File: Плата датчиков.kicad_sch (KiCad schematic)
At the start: 0 parts

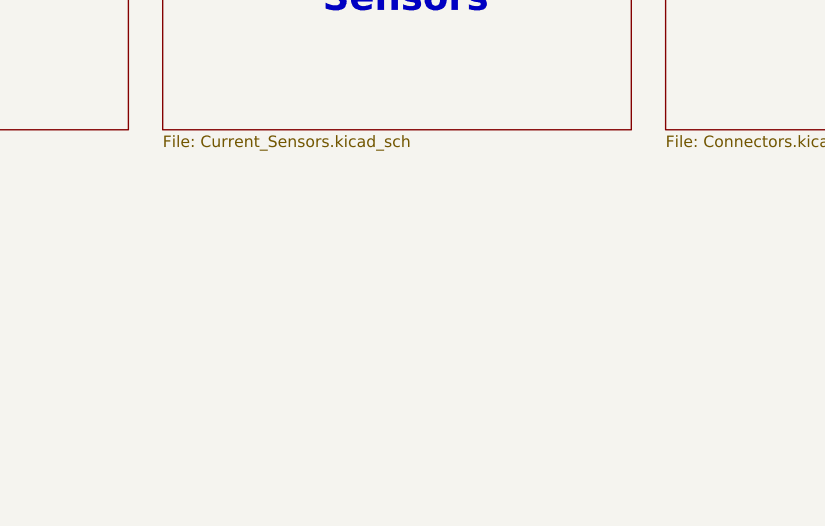
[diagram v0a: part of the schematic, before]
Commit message: Переместил силовые разъёмы
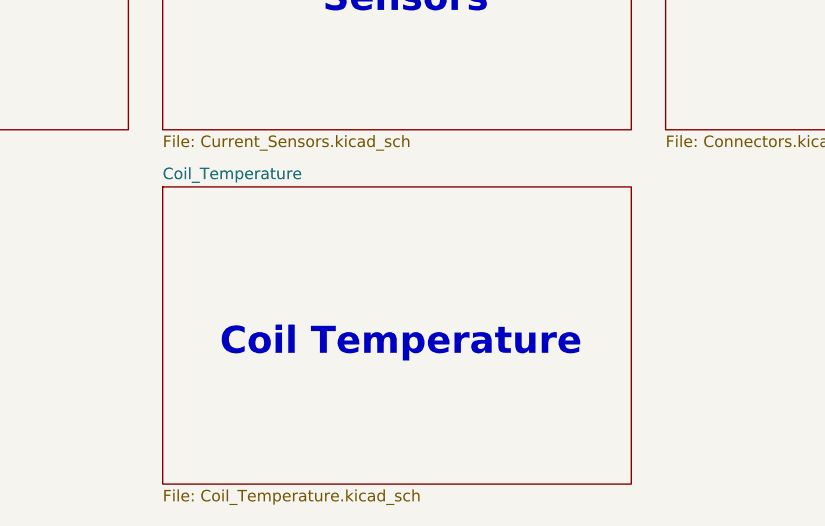
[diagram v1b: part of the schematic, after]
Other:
- added sheet Coil_Temperature (Coil_Temperature.kicad_sch)
- note added: "Coil Temperature"
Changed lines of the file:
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@@
+    (effects (font (size 3 3) (thickness 0.6) bold) (justify left bottom))
+  )
+  (text "Coil Temperature" (at 82.55 82.55 0)
     (effects (font (size 3 3) (thickness 0.6) bold) (justify left bottom))
   )
@@
       )
     )
+  )
+  (sheet (at 76.2 63.5) (size 52.07 33.02) (fields_autoplaced)
+    (stroke (width 0.1524) (type solid))
+    (fill (color 0 0 0 0.0000))
+    (property "Sheetname" "Coil_Temperature" (at 76.2 62.7884 0)
+      (effects (font (size 1.27 1.27)) (justify left bottom))
+    )
+    (property "Sheetfile" "Coil_Temperature.kicad_sch" (at 76.2 97.1046 0)
+      (effects (font (size 1.27 1.27)) (justify left top))
+    )
+    (property "Поле2" "" (at 76.2 63.5 0)
+      (effects (font (size 1.27 1.27)) hide)
+    )
+    (property "Поле3" "" (at 76.2 63.5 0)
+      (effects (font (size 1.27 1.27)) hide)
+    )
+    (instances
+      (project "Плата управления"
+        (path "/75f4c67c-bbde-4446-8f82-67797a1b269f" (page "7"))
+      )
+      (project "Плата датчиков"
+        (path "/69677e3f-3942-4c93-9a5c-92669e2df5eb" (page "5"))
+      )
+    )

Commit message: Добавил все документы
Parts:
- added C1, C2: 1n, Capacitor_SMD:C_0603_1608Metric_Pad1.08x0.95mm_HandSolder, symbol Device:C_Small
- added C10, C12, C14: 1u, Capacitor_SMD:C_0603_1608Metric_Pad1.08x0.95mm_HandSolder, symbol Device:C_Small
- added C11, C13, C17, C3, C4, C5: 100n, Capacitor_SMD:C_0603_1608Metric_Pad1.08x0.95mm_HandSolder, symbol Device:C_Small
- added C15, C18, C6, C8: 0.1u, Capacitor_SMD:C_0603_1608Metric_Pad1.08x0.95mm_HandSolder, symbol Device:C_Small
- added C16, C7, C9: 56p, Capacitor_SMD:C_0603_1608Metric_Pad1.08x0.95mm_HandSolder, symbol Device:C_Small
- added D1: NSM3012, Package_SO:SOIC-8_3.9x4.9mm_P1.27mm, symbol Hall_Sensor_My:NSM3012
- added J1: A, Connector_My:Power_Wire, symbol Connector_Generic:Conn_01x01
- added J10, J11, J12, J13, J14, J5, J6, J7, J9: 4900, Connector_My:4900, symbol 4900:4900
- added J2: B, Connector_My:Power_Wire, symbol Connector_Generic:Conn_01x01
- added J3: C, Connector_My:Power_Wire, symbol Connector_Generic:Conn_01x01
- added J4: Conn_02x07_Odd_Even, Connector_PinSocket_2.54mm:PinSocket_2x07_P2.54mm_Vertical, symbol Connector_Generic:Conn_02x07_Odd_Even
- added J8: Conn_02x02_Odd_Even, Connector_PinHeader_2.54mm:PinHeader_2x02_P2.54mm_Vertical, symbol Connector_Generic:Conn_02x02_Odd_Even
- added R1: 0, Resistor_SMD:R_0603_1608Metric_Pad0.98x0.95mm_HandSolder, symbol Device:R_Small
- added R10, R12, R14, R3, R6, R8: 120, Resistor_SMD:R_0603_1608Metric_Pad0.98x0.95mm_HandSolder, symbol Device:R_Small
- added R11, R13, R9: 15k, Resistor_SMD:R_0603_1608Metric_Pad0.98x0.95mm_HandSolder, symbol Device:R_Small
- added R15, R19, R20: 9.1k, Resistor_SMD:R_0603_1608Metric_Pad0.98x0.95mm_HandSolder, symbol Device:R_Small
- added R16, R17, R18: 1k, Resistor_SMD:R_0603_1608Metric_Pad0.98x0.95mm_HandSolder, symbol Device:R_Small
- added R2: 51, Resistor_SMD:R_0603_1608Metric_Pad0.98x0.95mm_HandSolder, symbol Device:R_Small
- added R4, R5, R7: 0.5m, Resistor_SMD:R_2512_6332Metric_Pad1.40x3.35mm_HandSolder, symbol Device:R
- added U1, U2, U3: INA282, Package_SO:SOIC-8_3.9x4.9mm_P1.27mm, symbol Amplifier_Current:INA283
- added U4: LMV324, Package_SO:SOIC-14_3.9x8.7mm_P1.27mm, symbol Amplifier_Operational:LMV324
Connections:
- new net: R6.2, U2.5
- new net: R3.2, U1.5
- new net: R15.1, R16.2, U4.6 (-)
- new net: R12.2, R15.2, U4.7
- new net: R10.2, R19.2, U4.1
- new net: C3.1, D1.1 (VDD), R1.2
- new net: R14.2, R20.2, U4.8
- new net: R18.2, R19.1, U4.2 (-)
- new net: C2.2, R2.1
- new net: C5.2, D1.7 (VLDO)
- new net: R8.2, U3.5
- new net: R17.2, R20.1, U4.9 (-)
- new net +3.3V: C1.1, C15.1, C6.1, C8.1, J4.1 (Pin_1), R1.1, U1.3 (REF2), U1.6 (V+), U2.3 (REF2), U2.6 (V+), U3.3 (REF2), U3.6 (V+)
- new net +3.3VA: C18.1, J4.13 (Pin_13), R11.1, R13.1, R9.1, U4.4 (V+)
- new net A: J1.1 (Pin_1), R4.1, U1.8 (+)
- new net A_OUT: J5.1, J5.2, J6.1, J6.2, J9.1, J9.2, R4.2, U1.1 (-)
- new net B: J2.1 (Pin_1), R5.1, U2.8 (+)
- new net B_OUT: J12.1, J12.2, J13.1, J13.2, J14.1, J14.2, R5.2, U2.1 (-)
- new net C: J3.1 (Pin_1), R7.1, U3.8 (+)
- new net CS_MCU: D1.5 (CS), J4.3 (Pin_3)
- new net C_OUT: J10.1, J10.2, J11.1, J11.2, J7.1, J7.2, R7.2, U3.1 (-)
- new net Current_A_MCU: C16.1, J4.12 (Pin_12), R3.1
- new net Current_B_MCU: C7.1, J4.11 (Pin_11), R6.1
- new net Current_C_MCU: C9.1, J4.10 (Pin_10), R8.1
- new net GND: C1.2, C15.2, C16.2, C2.1, C3.2, C4.1, C5.1, C6.2, C7.2, C8.2, C9.2, D1.8 (GND), J4.2 (Pin_2), U1.2 (GND), U1.7 (REF1), U2.2 (GND), U2.7 (REF1), U3.2 (GND), U3.7 (REF1)
- new net GNDA: C10.2, C11.2, C12.2, C13.2, C14.2, C17.2, C18.2, J4.14 (Pin_14), J8.2 (Pin_2), R16.1, R17.1, R18.1, U4.11 (V-)
- new net OUT_MCU: C4.2, D1.3 (OUT), J4.9 (Pin_9), R2.2
- new net PTC_Coil_A: C10.1, J8.1 (Pin_1), R9.2, U4.3 (+)
- new net PTC_Coil_B: C12.1, J8.4 (Pin_4), R11.2, U4.5 (+)
- new net PTC_Coil_C: C14.1, J8.3 (Pin_3), R13.2, U4.10 (+)
- new net SCLK_MCU: D1.4 (SCLK), J4.5 (Pin_5)
- new net SDIO_MCU: D1.6 (SDIO), J4.7 (Pin_7)
- new net Temp_Coil_A_MCU: C11.1, J4.8 (Pin_8), R10.1
- new net Temp_Coil_B_MCU: C13.1, J4.6 (Pin_6), R12.1
- new net Temp_Coil_C_MCU: C17.1, J4.4 (Pin_4), R14.1
- no-connect marks 0 -> 1
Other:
- removed sheet Coil_Temperature
- removed sheet Connectors
- removed sheet Current_Sensors
- removed sheet Rotary_Position_Sensor
- note added: "Датчик положения"
- note added: "Измерение тока А"
- note added: "Измерение тока В"
- note added: "Измерение тока С"
- note added: "Межплатные сигнальные разъёмы"
- note added: "Ножевые разъёмы"
- note added: "Питание ОУ"
- note added: "Температура обмотки B"
- note added: "Температура обмотки А"
- note added: "Температура обмотки С"
- note added: "Фазные разъёмы"
- note removed: "Coil Temperature"
- note removed: "Connectors"
- note removed: "Current Sensors"
- note removed: "Rotary Position Sensor"
- title: (none) -> Плата датчиков

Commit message: ...
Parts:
- removed C1, C2: 1n, Capacitor_SMD:C_0603_1608Metric_Pad1.08x0.95mm_HandSolder, symbol Device:C_Small
- removed C10, C12, C14: 1u, Capacitor_SMD:C_0603_1608Metric_Pad1.08x0.95mm_HandSolder, symbol Device:C_Small
- removed C11, C13, C17, C3, C4, C5: 100n, Capacitor_SMD:C_0603_1608Metric_Pad1.08x0.95mm_HandSolder, symbol Device:C_Small
- removed C15, C18, C6, C8: 0.1u, Capacitor_SMD:C_0603_1608Metric_Pad1.08x0.95mm_HandSolder, symbol Device:C_Small
- removed C16, C7, C9: 56p, Capacitor_SMD:C_0603_1608Metric_Pad1.08x0.95mm_HandSolder, symbol Device:C_Small
- removed D1: NSM3012, Package_SO:SOIC-8_3.9x4.9mm_P1.27mm, symbol Hall_Sensor_My:NSM3012
- removed J1: A, Connector_My:Power_Wire, symbol Connector_Generic:Conn_01x01
- removed J10, J11, J12, J13, J14, J5, J6, J7, J9: 4900, Connector_My:4900, symbol 4900:4900
- removed J2: B, Connector_My:Power_Wire, symbol Connector_Generic:Conn_01x01
- removed J3: C, Connector_My:Power_Wire, symbol Connector_Generic:Conn_01x01
- removed J4: Conn_02x07_Odd_Even, Connector_PinSocket_2.54mm:PinSocket_2x07_P2.54mm_Vertical, symbol Connector_Generic:Conn_02x07_Odd_Even
- removed J8: Conn_02x02_Odd_Even, Connector_PinHeader_2.54mm:PinHeader_2x02_P2.54mm_Vertical, symbol Connector_Generic:Conn_02x02_Odd_Even
- removed R1: 0, Resistor_SMD:R_0603_1608Metric_Pad0.98x0.95mm_HandSolder, symbol Device:R_Small
- removed R10, R12, R14, R3, R6, R8: 120, Resistor_SMD:R_0603_1608Metric_Pad0.98x0.95mm_HandSolder, symbol Device:R_Small
- removed R11, R13, R9: 15k, Resistor_SMD:R_0603_1608Metric_Pad0.98x0.95mm_HandSolder, symbol Device:R_Small
- removed R15, R19, R20: 9.1k, Resistor_SMD:R_0603_1608Metric_Pad0.98x0.95mm_HandSolder, symbol Device:R_Small
- removed R16, R17, R18: 1k, Resistor_SMD:R_0603_1608Metric_Pad0.98x0.95mm_HandSolder, symbol Device:R_Small
- removed R2: 51, Resistor_SMD:R_0603_1608Metric_Pad0.98x0.95mm_HandSolder, symbol Device:R_Small
- removed R4, R5, R7: 0.5m, Resistor_SMD:R_2512_6332Metric_Pad1.40x3.35mm_HandSolder, symbol Device:R
- removed U1, U2, U3: INA282, Package_SO:SOIC-8_3.9x4.9mm_P1.27mm, symbol Amplifier_Current:INA283
- removed U4: LMV324, Package_SO:SOIC-14_3.9x8.7mm_P1.27mm, symbol Amplifier_Operational:LMV324
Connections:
- no-connect marks 1 -> 0
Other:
- added sheet Conection_list (Conection_list.kicad_sch)
- added sheet Connectors (Connectors.kicad_sch)
- added sheet Current_Sensoors (Curret_Sensors.kicad_sch)
- added sheet Rotary_Position_Sensor (Rotary_Position_Sensor.kicad_sch)
- added sheet Temperature (Temperature.kicad_sch)
- note added: "Схема электрическая"
- note added: "принципиальная"
- note removed: "Датчик положения"
- note removed: "Измерение тока А"
- note removed: "Измерение тока В"
- note removed: "Измерение тока С"
- note removed: "Межплатные сигнальные разъёмы"
- note removed: "Ножевые разъёмы"
- note removed: "Питание ОУ"
- note removed: "Температура обмотки B"
- note removed: "Температура обмотки А"
- note removed: "Температура обмотки С"
- note removed: "Фазные разъёмы"
- title: Плата датчиков -> Измерительный узел

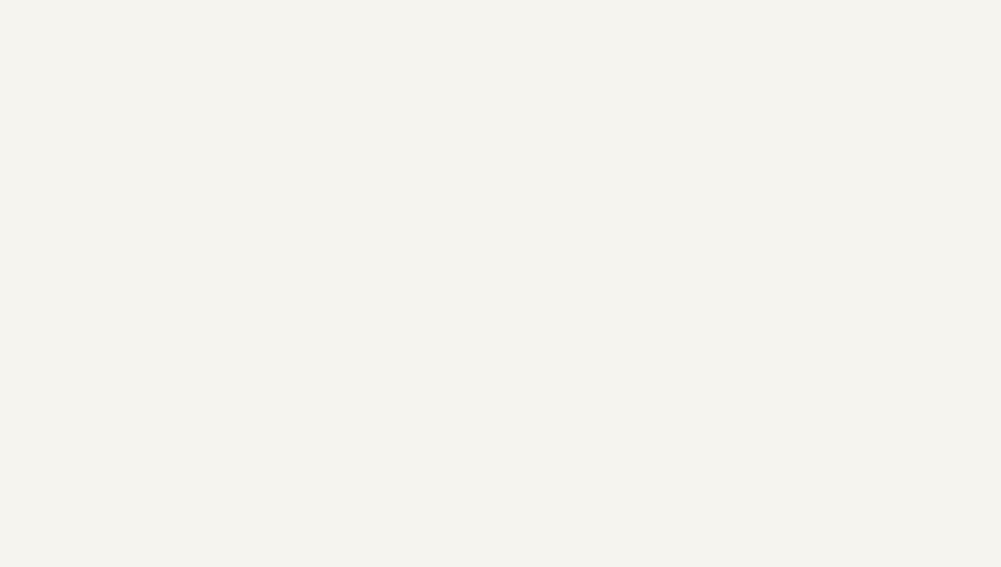
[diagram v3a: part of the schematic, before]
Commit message: Изменил разводку шунтов, вывел выход датчика положения после фильтра
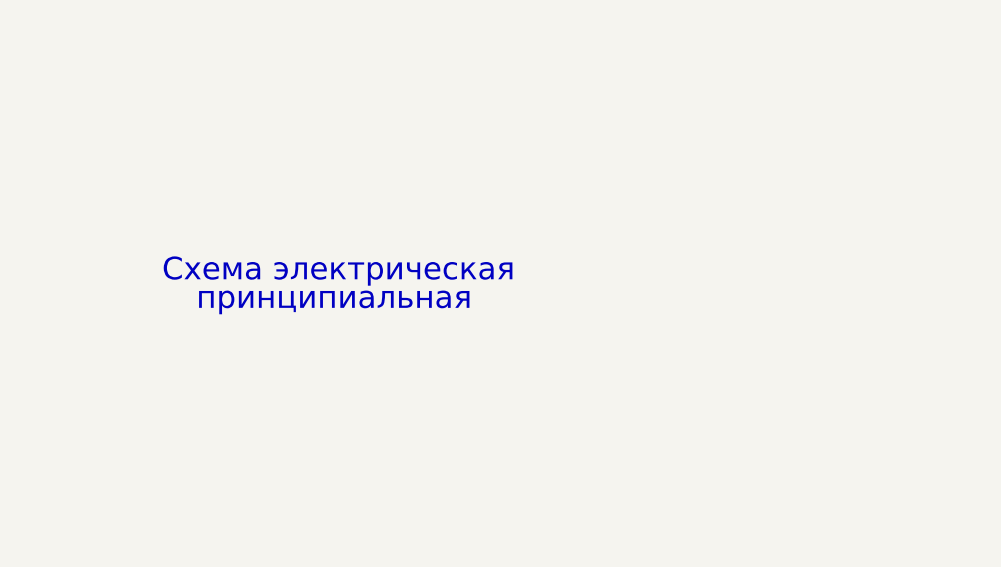
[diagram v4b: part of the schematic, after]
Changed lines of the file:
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@@
     (title "Измерительный узел")
     (date "2023-12-14")
-    (comment 1 "МПСТ.76721.758764.03.Э3.М")
+    (comment 1 "МПСТ.76721.758764.03.М Э3")
     (comment 2 "Филатов")
     (comment 3 "Нестеров")
@@
     (comment 6 "Саяхов")
   )
+  (text "Схема электрическая\n" (at 189.865 183.515 0)
+    (effects (font (size 2.5 2.5)) (justify left bottom))
+  )
+  (text "принципиальная\n" (at 193.675 186.69 0)
+    (effects (font (size 2.5 2.5)) (justify left bottom))
+  )
   (text "Схема электрическая" (at 313.055 272.415 0)
